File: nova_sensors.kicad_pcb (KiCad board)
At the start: 2 copper layers, 100 x 82.5 mm, 93 parts, among them J1 Conn_01x03_Socket, J10 Conn_01x04_Socket, J11 Conn_01x04_Socket, J2 Conn_01x03_Socket, J3 Conn_01x04_Socket, J4 Conn_01x02_Socket, J5 Conn_01x02_Socket, J6 Conn_01x03_Socket, J7 Conn_01x02_Socket, J8 Conn_01x02_Socket, J9 Conn_01x02_Socket, SW1 SW_Push, SW2 SW_DIP_x02, SW3 SW_DIP_x02, U1 AT32F455CET7, U2 MAX3232, U3 MAX13488, U4 MAX13488, U5 LD1117S33TR, U6 XL1509-ADJ, Y1 8Mhz, Y2 32768hz

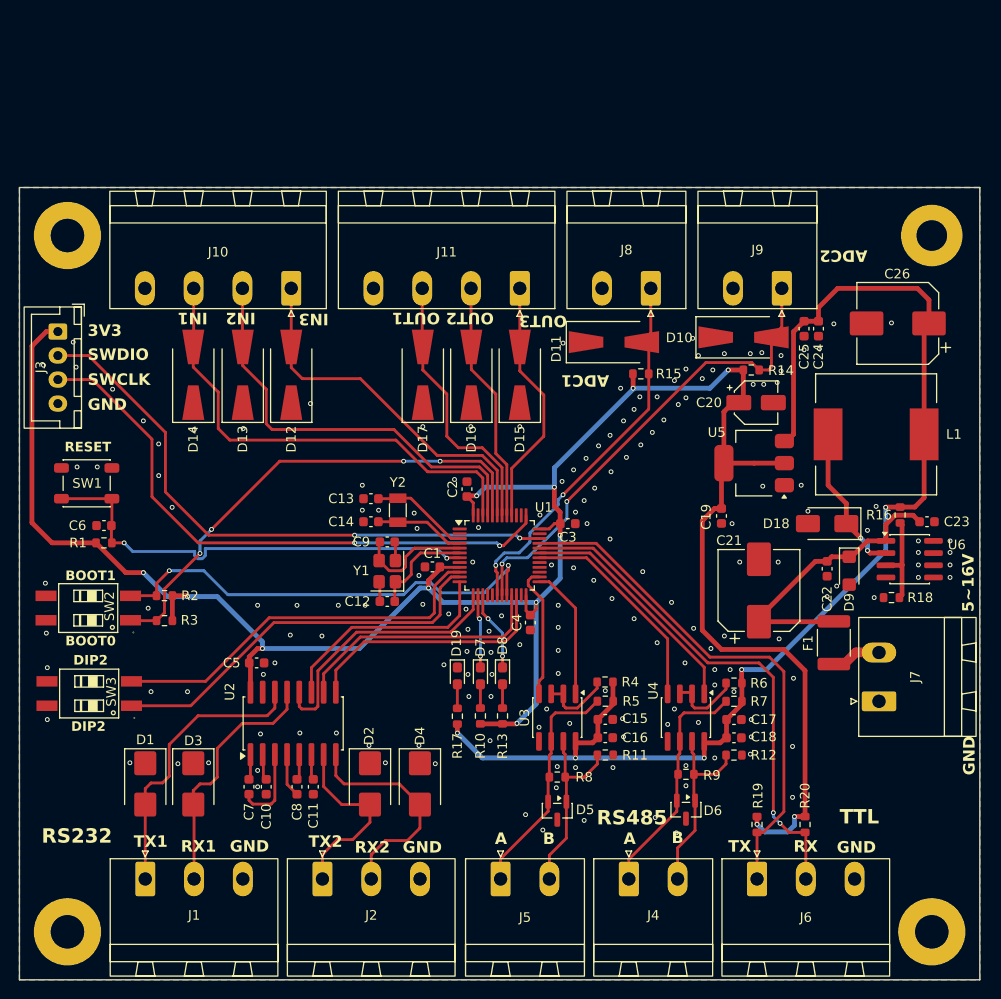
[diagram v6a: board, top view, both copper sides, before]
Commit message: fix: 微调丝印位置
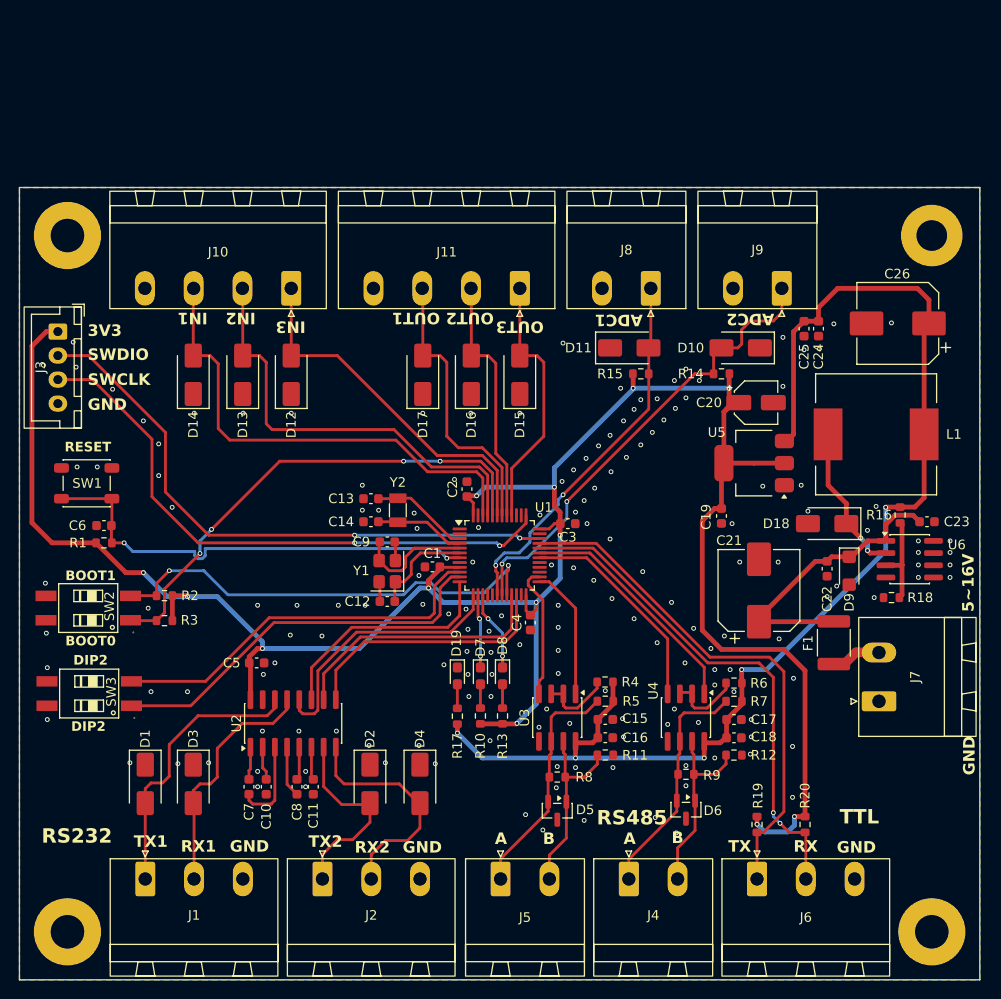
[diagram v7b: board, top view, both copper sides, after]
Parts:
- D1, D2, D3, D4: footprint Diode_SMD:D_SMB -> Diode_SMD:D_SMA
- D10, D11, D12, D13, D14, D15, D16, D17: footprint Diode_SMD:D_SMA-SMB_Universal_Handsoldering -> Diode_SMD:D_SMA
- U2: footprint Package_SO:SOIC-16W_5.3x10.2mm_P1.27mm -> Package_SO:SOIC-16_3.9x9.9mm_P1.27mm
- moved R14 3.13 mm to (73.1, 146.9), turned to 180 degrees
- moved D11 1.71 mm to (63.5, 144.2)
- moved D10 1.14 mm to (75.1, 144.2), turned to 180 degrees
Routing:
- net /ADC2: track 50.0 -> 48.7 mm
- net /OUT3: track 26.1 -> 27.1 mm
- net /OUT1: track 28.5 -> 29.6 mm
- net /IN1: track 49.3 -> 50.3 mm
- net /OUT2: track 25.2 -> 26.2 mm
- net /IN2: track 44.6 -> 45.6 mm
- net Net-(U2-VS-): track 2.66 -> 3.43 mm
- net Net-(U2-VS+): track 2.73 -> 3.51 mm
- net Net-(U2-C2-): track 2.67 -> 3.45 mm
- net Net-(U2-C2+): track 4.55 -> 5.33 mm
- net Net-(U2-C1-): track 8.40 -> 9.18 mm
- net Net-(U2-C1+): track 2.64 -> 3.41 mm
- net Net-(D4-A2): track 23.4 -> 24.2 mm
- net Net-(D2-A2): track 19.7 -> 20.4 mm
- net /232_2_TX: track 26.9 -> 27.7 mm
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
